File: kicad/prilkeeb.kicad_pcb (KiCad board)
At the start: 2 copper layers, 176.5 x 142.7 mm, 73 parts, among them U2 Nice_Nano_V2

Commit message: Update design
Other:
- board outline removed

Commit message: Update pcb
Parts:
- moved D34 57.2 mm to (118.1, 138.1)
- moved D33 38.2 mm to (118.1, 133.3)
- moved D29 37.2 mm to (66.7, 150.5), turned to 90 degrees
- moved D30 26.1 mm to (85.7, 150.5), turned to 90 degrees
- moved D31 22.4 mm to (104.8, 150.5), turned to 90 degrees
- moved D35 21.7 mm to (118.1, 142.9)
- moved D22 6.23 mm to (54.8, 133.3)
- moved D32 0.59 mm to (118.1, 128.6)
- turned S32 to 168 degrees
- turned S33 to 78 degrees
- turned S34 to 78 degrees
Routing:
- net Col_1: track 0.00 -> 272.1 mm, vias 0 -> 12
- net Col_4: track 0.00 -> 271.4 mm, vias 0 -> 6
- net Col_3: track 0.00 -> 228.3 mm, vias 0 -> 8
- net Col_2: track 0.00 -> 217.1 mm, vias 0 -> 10
- net Col_5: track 0.00 -> 207.2 mm, vias 0 -> 2
- net Row_4: track 0.00 -> 195.8 mm
- net Col_6: track 0.00 -> 190.1 mm, vias 0 -> 2
- net Row_5: track 0.00 -> 189.9 mm
- net Row_3: track 0.00 -> 182.1 mm
- net Col_7: track 0.00 -> 181.3 mm
- net Row_2: track 0.00 -> 163.4 mm
- net Row_1: track 0.00 -> 143.5 mm
- net Net-(D34-A): track 0.00 -> 88.6 mm
- net Net-(D33-A): track 0.00 -> 71.5 mm
- net Net-(D32-A): track 0.00 -> 53.4 mm
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
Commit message: Update design
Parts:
- added RST_SW_L1: SW_Push, Button_Switch_SMD:SW_SPST_SKQG_WithStem, F.Cu at (131.5, 138.5)
- added RST_SW_R1: SW_Push, Button_Switch_SMD:SW_SPST_SKQG_WithStem, B.Cu at (131.5, 138.5)
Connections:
- U2 pad 21: unconnected-(U2-3.3v-Pad21) -> VCC
- U2 pad 22: unconnected-(U2-RST-Pad22) -> RST
- U2 pad 23: unconnected-(U2-GND-Pad23) -> GND
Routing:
- net RST: track 0.00 -> 169.7 mm, vias 0 -> 2
- net GND: track 0.00 -> 167.2 mm, vias 0 -> 3
- net Net-(D34-A): track 88.6 -> 92.0 mm
- net Net-(D35-A): track 46.1 -> 47.1 mm
- net Col_4: track 271.4 -> 270.5 mm
- net Row_5: track 189.9 -> 190.8 mm
- net Col_3: track 228.3 -> 227.7 mm
- added copper zone on B.Cu, net (none)
- added copper zone on F.Cu, net (none)
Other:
- board outline added: 176.1 x 134.6 mm

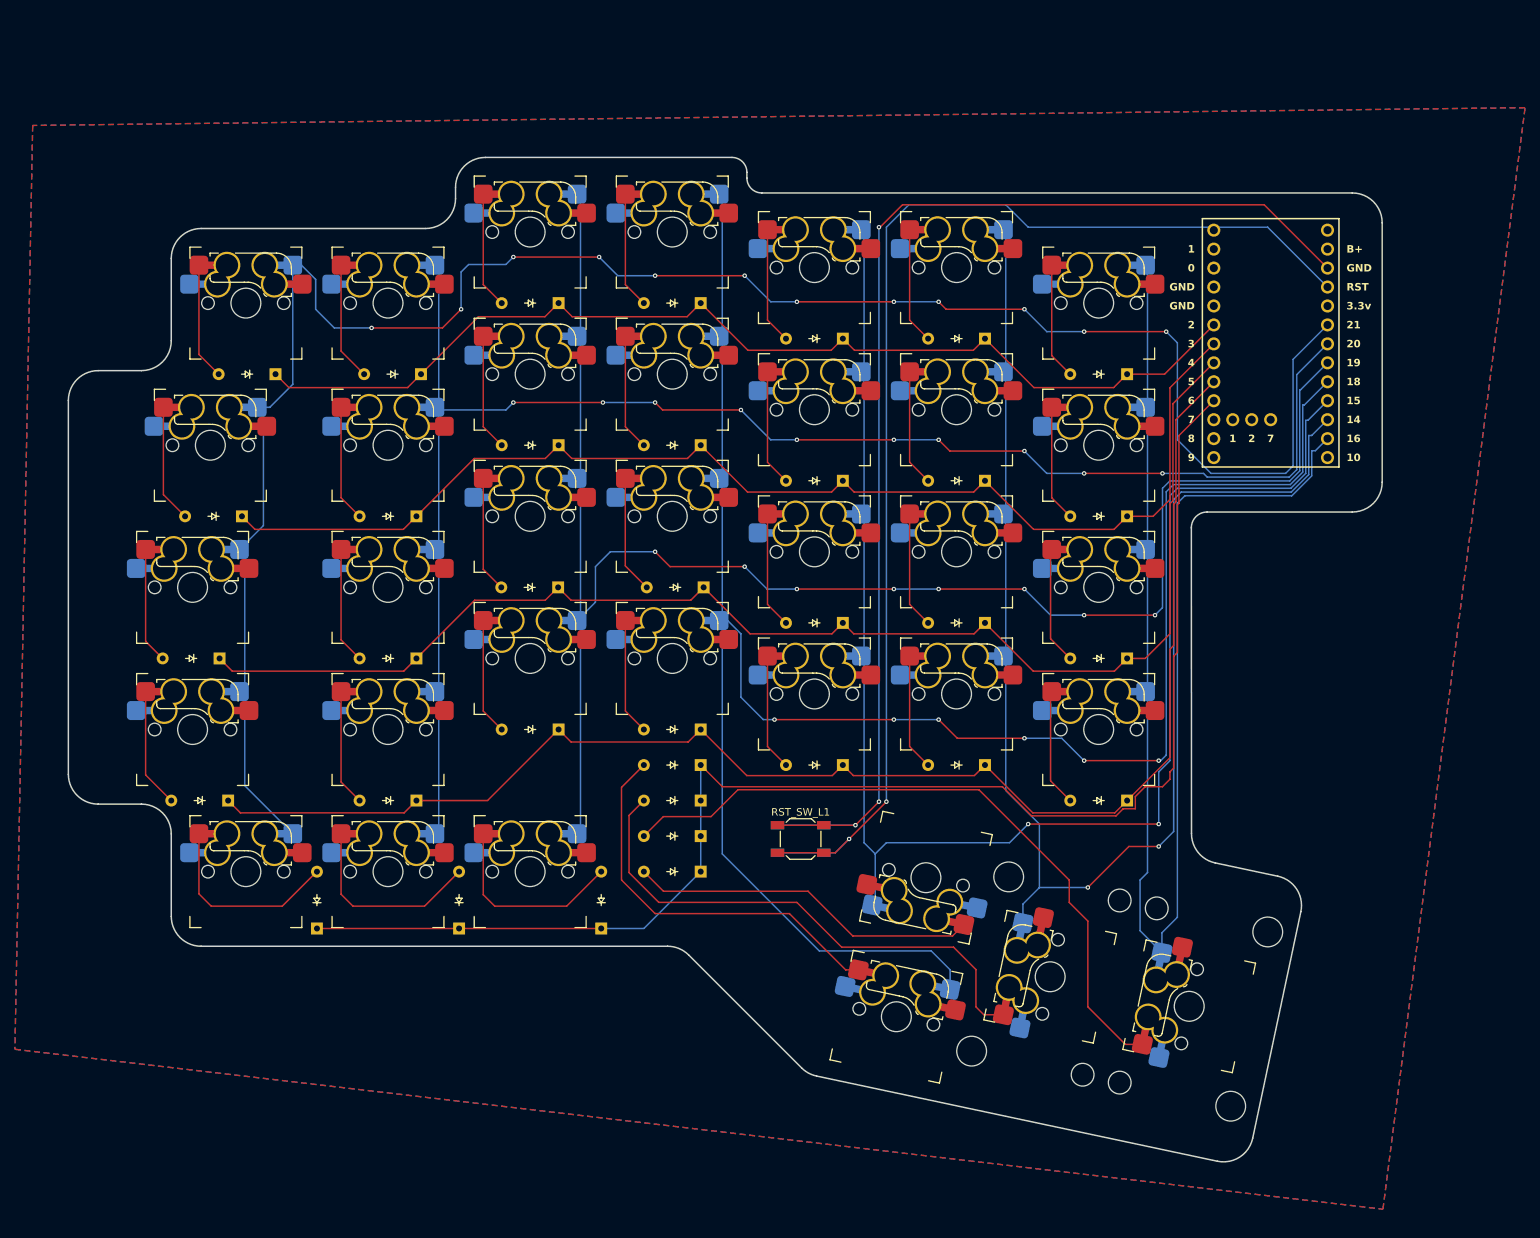
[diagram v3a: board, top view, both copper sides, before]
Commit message: Update MCU position
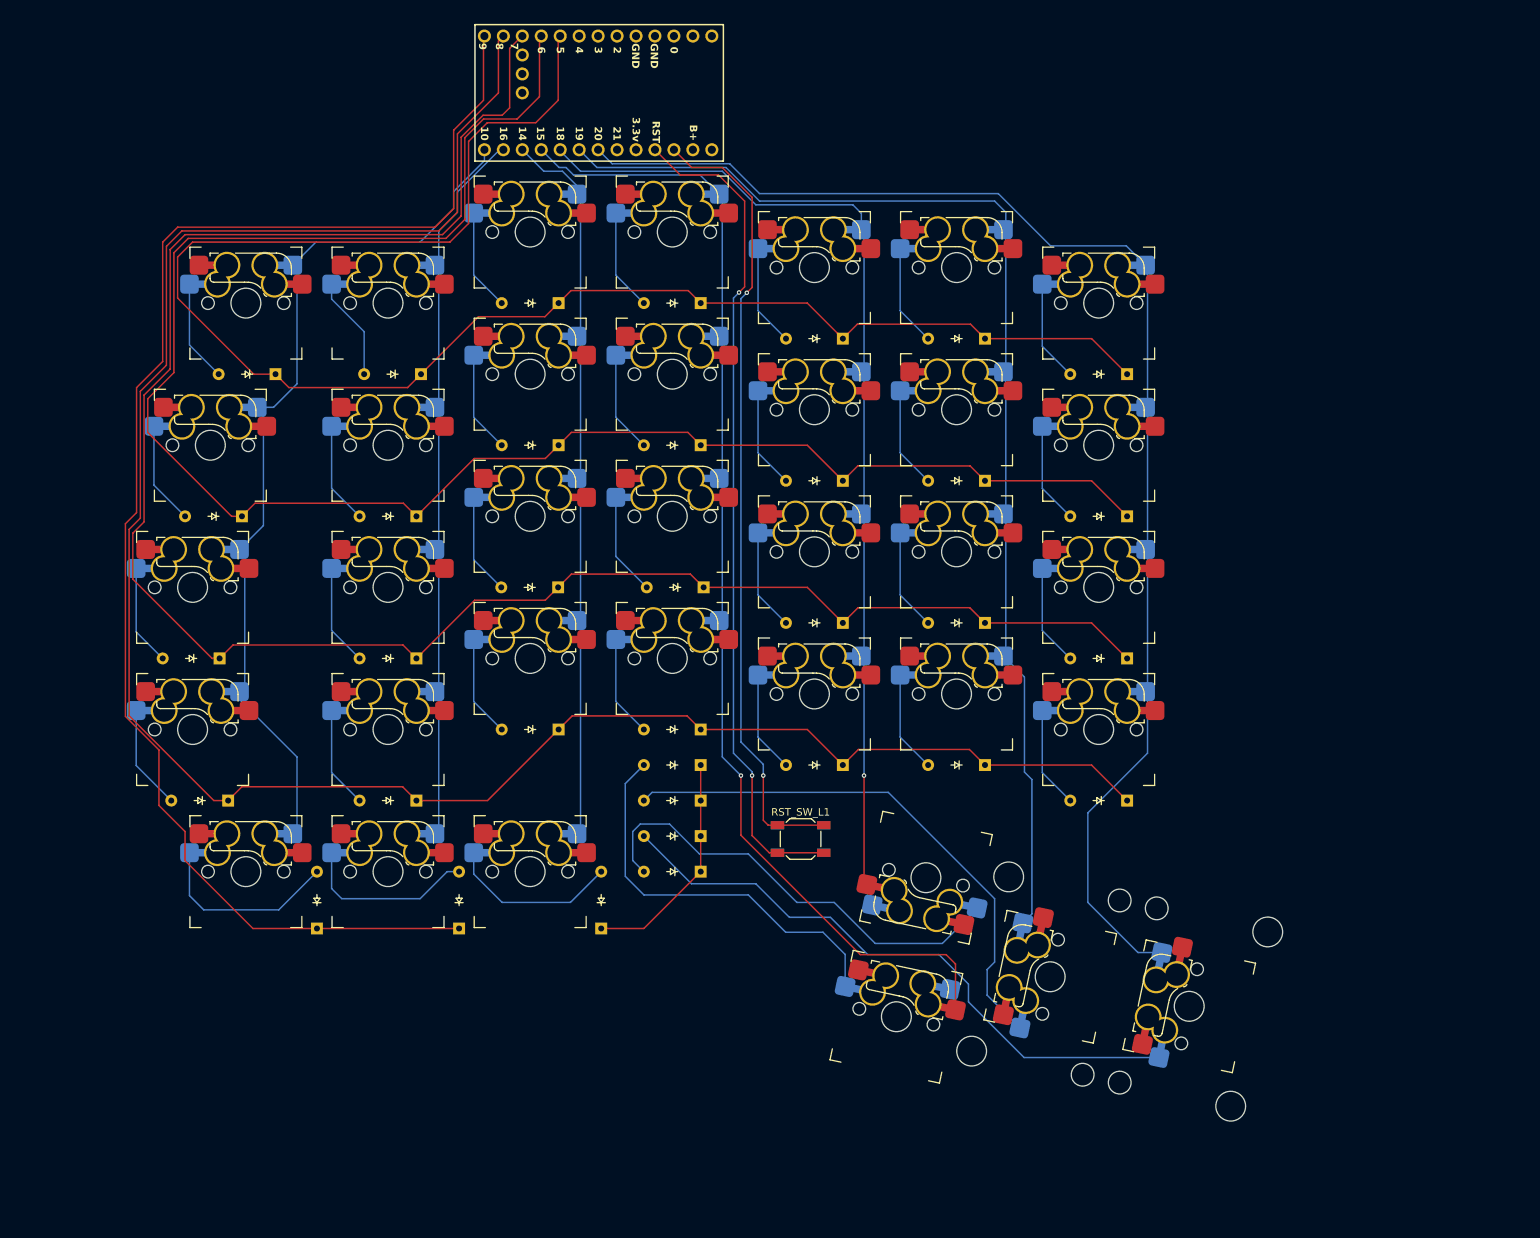
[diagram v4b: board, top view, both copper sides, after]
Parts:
- moved U2 97.5 mm to (103.4, 38.5), turned to -90 degrees
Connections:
- D1 pad 1: Row_1 -> Row_0
- D10 pad 1: Row_2 -> Row_1
- D11 pad 1: Row_2 -> Row_1
- D12 pad 1: Row_2 -> Row_1
- D13 pad 1: Row_2 -> Row_1
- D14 pad 1: Row_2 -> Row_1
- D15 pad 1: Row_3 -> Row_2
- D16 pad 1: Row_3 -> Row_2
- D17 pad 1: Row_3 -> Row_2
- D18 pad 1: Row_3 -> Row_2
- D19 pad 1: Row_3 -> Row_2
- D2 pad 1: Row_1 -> Row_0
- D20 pad 1: Row_3 -> Row_2
- D21 pad 1: Row_3 -> Row_2
- D22 pad 1: Row_4 -> Row_3
- D23 pad 1: Row_4 -> Row_3
- D24 pad 1: Row_4 -> Row_3
- D25 pad 1: Row_4 -> Row_3
- D26 pad 1: Row_4 -> Row_3
- D27 pad 1: Row_4 -> Row_3
- D28 pad 1: Row_4 -> Row_3
- D29 pad 1: Row_5 -> Row_4
- D3 pad 1: Row_1 -> Row_0
- D30 pad 1: Row_5 -> Row_4
- D31 pad 1: Row_5 -> Row_4
- D32 pad 1: Row_5 -> Row_4
- D33 pad 1: Row_5 -> Row_4
- D34 pad 1: Row_5 -> Row_4
- D35 pad 1: Row_5 -> Row_4
- D4 pad 1: Row_1 -> Row_0
- D5 pad 1: Row_1 -> Row_0
- D6 pad 1: Row_1 -> Row_0
- D7 pad 1: Row_1 -> Row_0
- D8 pad 1: Row_2 -> Row_1
- D9 pad 1: Row_2 -> Row_1
- S1 pad 1: Col_3 -> Col_2
- S10 pad 1: Col_5 -> Col_4
- S11 pad 1: Col_6 -> Col_5
- S12 pad 1: Col_1 -> Col_0
- S13 pad 1: Col_2 -> Col_1
- S14 pad 1: Col_7 -> Col_6
- S15 pad 1: Col_3 -> Col_2
- S16 pad 1: Col_4 -> Col_3
- S17 pad 1: Col_5 -> Col_4
- S18 pad 1: Col_6 -> Col_5
- S19 pad 1: Col_1 -> Col_0
- S2 pad 1: Col_4 -> Col_3
- S20 pad 1: Col_2 -> Col_1
- S21 pad 1: Col_7 -> Col_6
- S22 pad 1: Col_3 -> Col_2
- S23 pad 1: Col_4 -> Col_3
- S24 pad 1: Col_5 -> Col_4
- S25 pad 1: Col_6 -> Col_5
- S26 pad 1: Col_1 -> Col_0
- S27 pad 1: Col_2 -> Col_1
- S28 pad 1: Col_7 -> Col_6
- S29 pad 1: Col_1 -> Col_0
- S3 pad 1: Col_5 -> Col_4
- S30 pad 1: Col_2 -> Col_1
- S31 pad 1: Col_3 -> Col_2
- S32 pad 1: Col_5 -> Col_4
- S33 pad 1: Col_6 -> Col_5
- S34 pad 1: Col_7 -> Col_6
- S35 pad 1: Col_4 -> Col_3
- S4 pad 1: Col_6 -> Col_5
- S5 pad 1: Col_1 -> Col_0
- S6 pad 1: Col_2 -> Col_1
- S7 pad 1: Col_7 -> Col_6
- S8 pad 1: Col_3 -> Col_2
- S9 pad 1: Col_4 -> Col_3
- U2 pad 10: unconnected-(U2-7-Pad10) -> Row_2
- U2 pad 11: unconnected-(U2-8-Pad11) -> Row_3
- U2 pad 12: unconnected-(U2-9-Pad12) -> Row_4
- U2 pad 13: unconnected-(U2-10-Pad13) -> Col_0
- U2 pad 14: Col_7 -> Col_1
- U2 pad 15: Col_6 -> Col_2
- U2 pad 16: Col_5 -> Col_3
- U2 pad 18: Col_3 -> Col_5
- U2 pad 19: Col_2 -> Col_6
- U2 pad 20: Col_1 -> unconnected-(U2-21-Pad20)
- U2 pad 24: unconnected-(U2-B+-Pad24) -> (no net)
- U2 pad 5: Row_1 -> unconnected-(U2-2-Pad5)
- U2 pad 6: Row_2 -> unconnected-(U2-3-Pad6)
- U2 pad 7: Row_3 -> unconnected-(U2-4-Pad7)
- U2 pad 8: Row_4 -> Row_0
- U2 pad 9: Row_5 -> Row_1
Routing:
- net Row_0: track 0.00 -> 224.2 mm
- net Row_5: track 190.8 -> 0.00 mm
- net Col_7: track 181.3 -> 0.00 mm
- net Col_1: track 272.1 -> 97.5 mm, vias 12 -> 0
- net Col_4: track 270.5 -> 135.1 mm, vias 6 -> 1
- net Col_0: track 0.00 -> 119.9 mm
- net Col_2: track 217.1 -> 97.7 mm, vias 10 -> 0
- net Row_2: track 163.4 -> 266.4 mm
- net Row_1: track 143.5 -> 246.2 mm
- net Row_3: track 182.1 -> 283.2 mm
- net Col_3: track 227.7 -> 156.5 mm, vias 8 -> 1
- net GND: track 167.2 -> 106.9 mm, vias 3 -> 2
- net RST: track 169.7 -> 112.1 mm
- net Col_5: track 207.2 -> 158.9 mm, vias 2 -> 0
- net Row_4: track 195.8 -> 225.3 mm
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- removed copper zone on B.Cu, net (none)
- removed copper zone on F.Cu, net (none)
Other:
- board outline removed

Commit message: Adapt new design
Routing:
- net Row_4: track 225.3 -> 244.3 mm
- net RST: track 112.1 -> 122.7 mm, vias 2 -> 3
- net GND: track 106.9 -> 115.2 mm, vias 2 -> 3
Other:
- board outline added: 165.3 x 153.6 mm

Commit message: Add hole
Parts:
- added REF**: MountingHole_2.2mm_M2, MountingHole:MountingHole_2.2mm_M2, F.Cu at (130.5, 166.5)
- added REF**: MountingHole_2.2mm_M2, MountingHole:MountingHole_2.2mm_M2, F.Cu at (142.9, 109.5)
- added REF**: MountingHole_2.2mm_M2, MountingHole:MountingHole_2.2mm_M2, F.Cu at (182.0, 114.5)
- added REF**: MountingHole_2.2mm_M2, MountingHole:MountingHole_2.2mm_M2, F.Cu at (142.9, 71.4)
- added REF**: MountingHole_2.2mm_M2, MountingHole:MountingHole_2.2mm_M2, F.Cu at (188.0, 181.5)
- added REF**: MountingHole_2.2mm_M2, MountingHole:MountingHole_2.2mm_M2, F.Cu at (151.0, 132.5)
- added REF**: MountingHole_2.2mm_M2, MountingHole:MountingHole_2.2mm_M2, F.Cu at (42.5, 64.5)
- added REF**: MountingHole_2.2mm_M2, MountingHole:MountingHole_2.2mm_M2, F.Cu at (196.0, 144.0)
- added REF**: MountingHole_2.2mm_M2, MountingHole:MountingHole_2.2mm_M2, F.Cu at (64.3, 95.2)
- added REF**: MountingHole_2.2mm_M2, MountingHole:MountingHole_2.2mm_M2, F.Cu at (42.5, 142.5)
- added REF**: MountingHole_2.2mm_M2, MountingHole:MountingHole_2.2mm_M2, F.Cu at (182.0, 76.2)
- added REF**: MountingHole_2.2mm_M2, MountingHole:MountingHole_2.2mm_M2, F.Cu at (104.8, 126.2)
- added REF**: MountingHole_2.2mm_M2, MountingHole:MountingHole_2.2mm_M2, F.Cu at (104.8, 66.7)
- RST_SW_L1, RST_SW_R1: value SW_Push -> Reset
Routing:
- net Row_1: track 246.2 -> 248.2 mm
- net Row_0: track 224.2 -> 225.9 mm
- net GND: track 115.2 -> 116.2 mm
- net Row_2: track 266.4 -> 267.2 mm
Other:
- board size 165.3 x 153.6 mm -> 165.9 x 156.6 mm
